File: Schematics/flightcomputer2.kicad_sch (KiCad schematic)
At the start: 0 parts

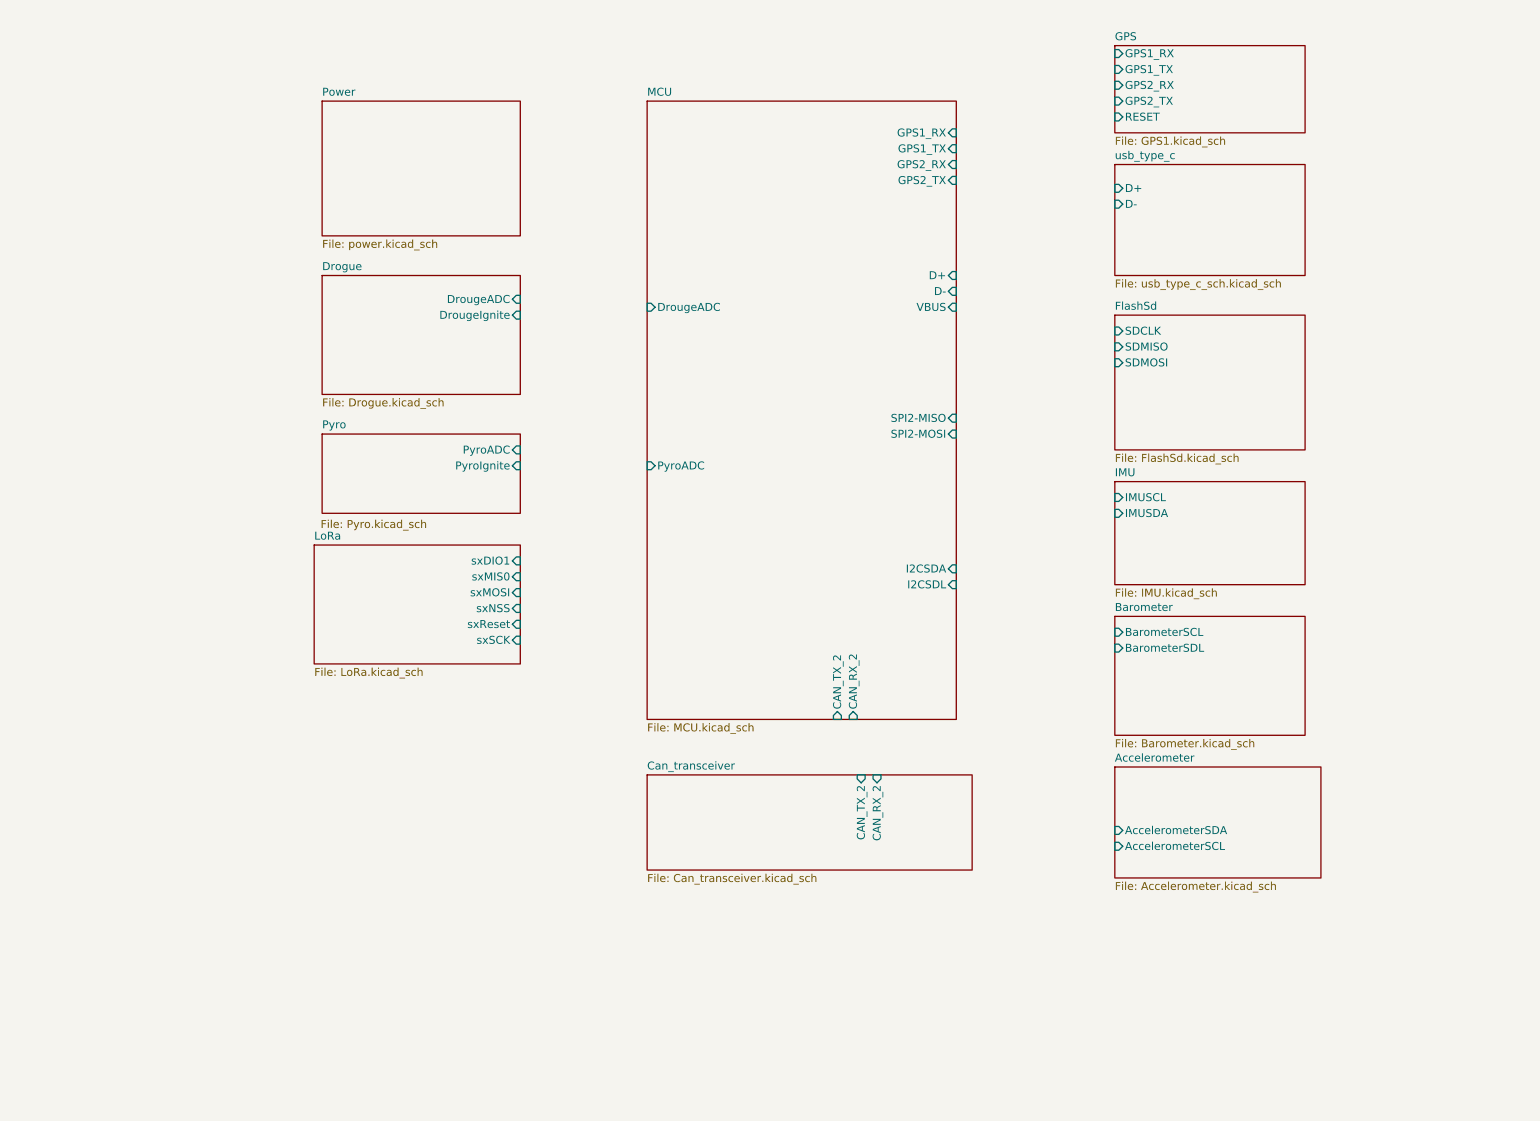
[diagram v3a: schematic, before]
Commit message: finished pin assignments and ran ERC all good ready for layout
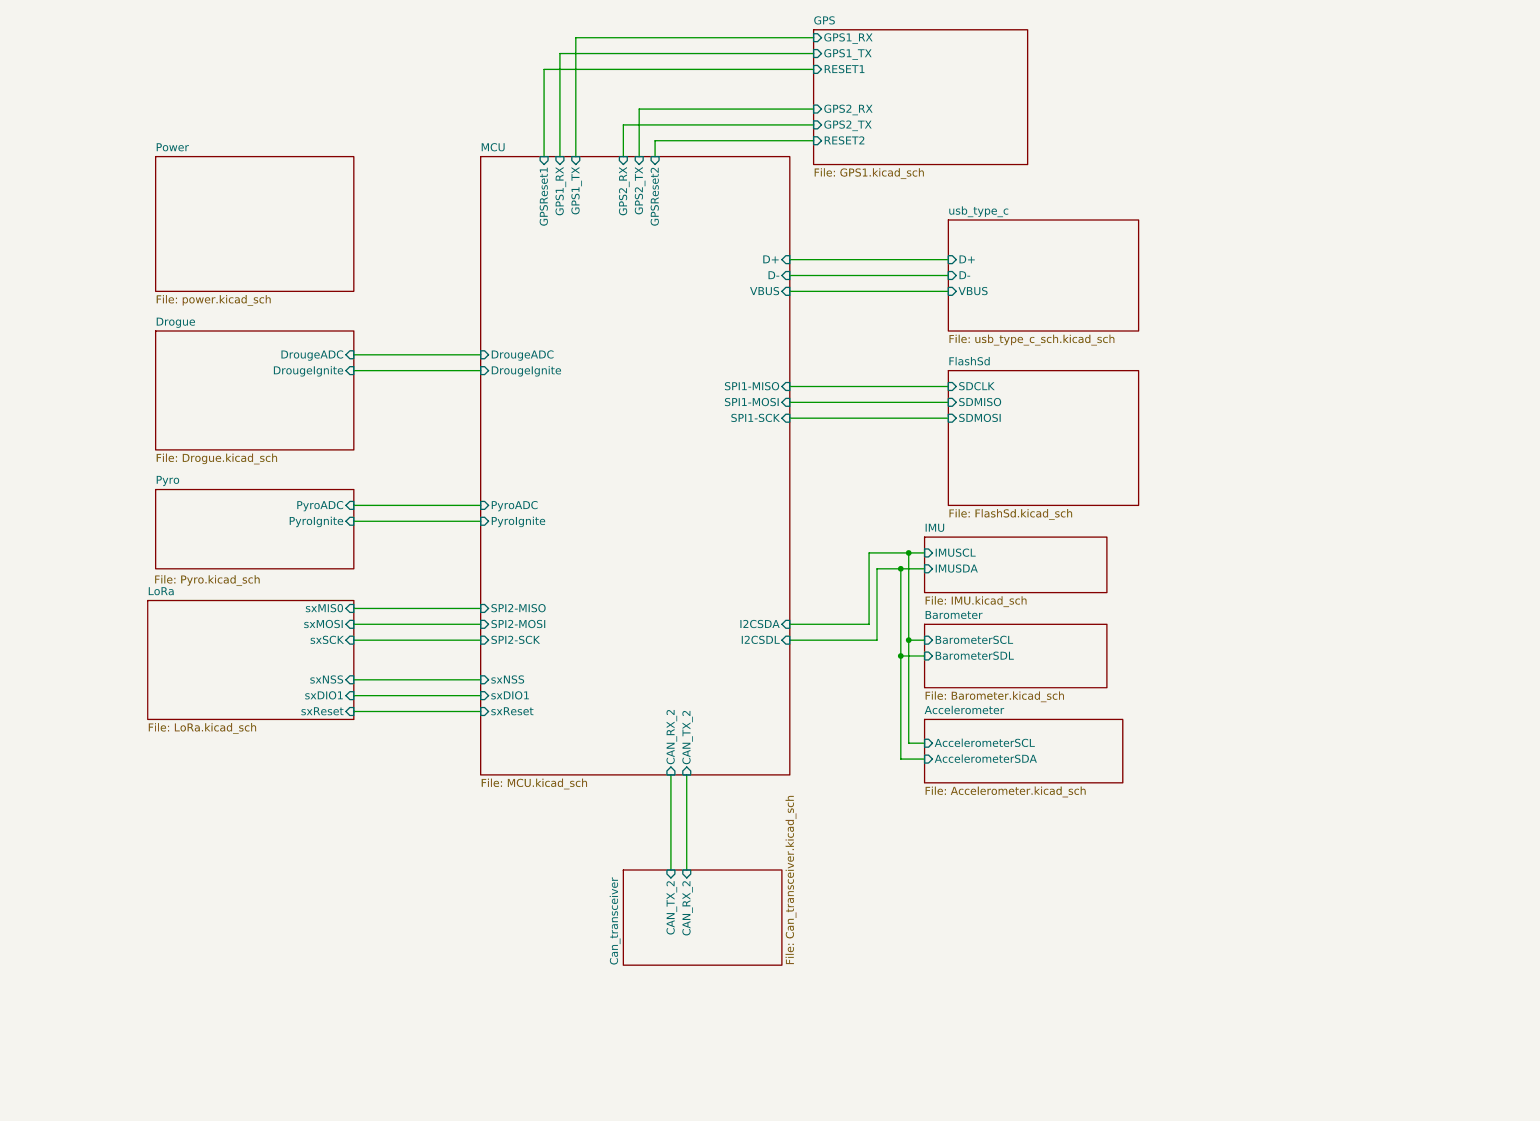
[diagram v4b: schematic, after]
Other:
- sheet GPS ports: added RESET1, RESET2; removed RESET
- sheet MCU ports: added DrougeIgnite, GPSReset1, GPSReset2, PyroIgnite, SPI1-MISO, SPI1-MOSI, SPI1-SCK, SPI2-SCK, sxDIO1, sxNSS, sxReset; removed none
- sheet usb_type_c ports: added VBUS; removed none

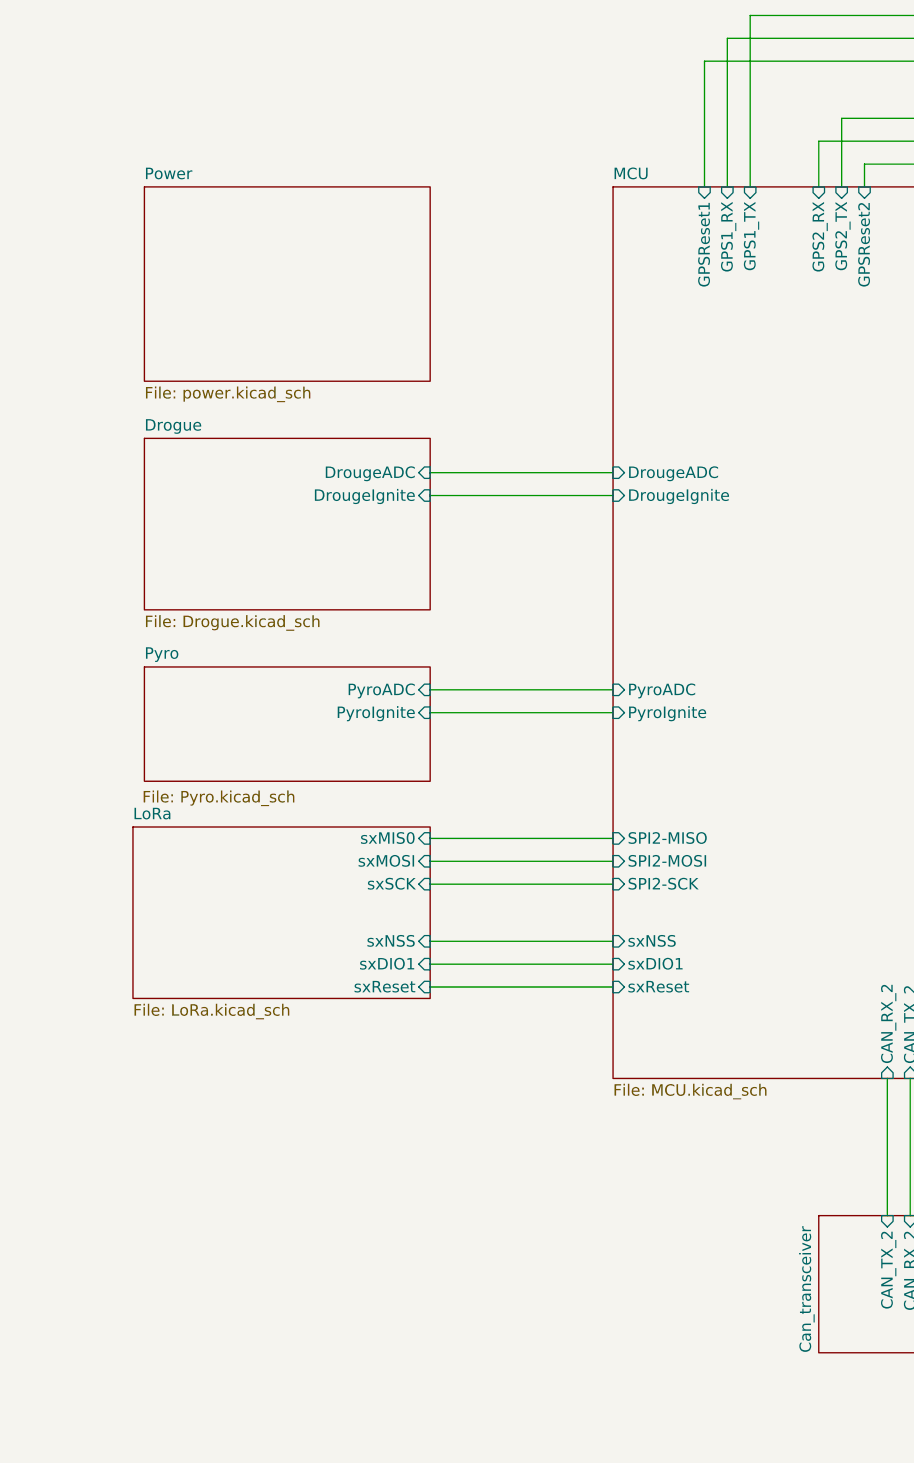
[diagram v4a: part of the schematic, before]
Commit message: Added Flash memory
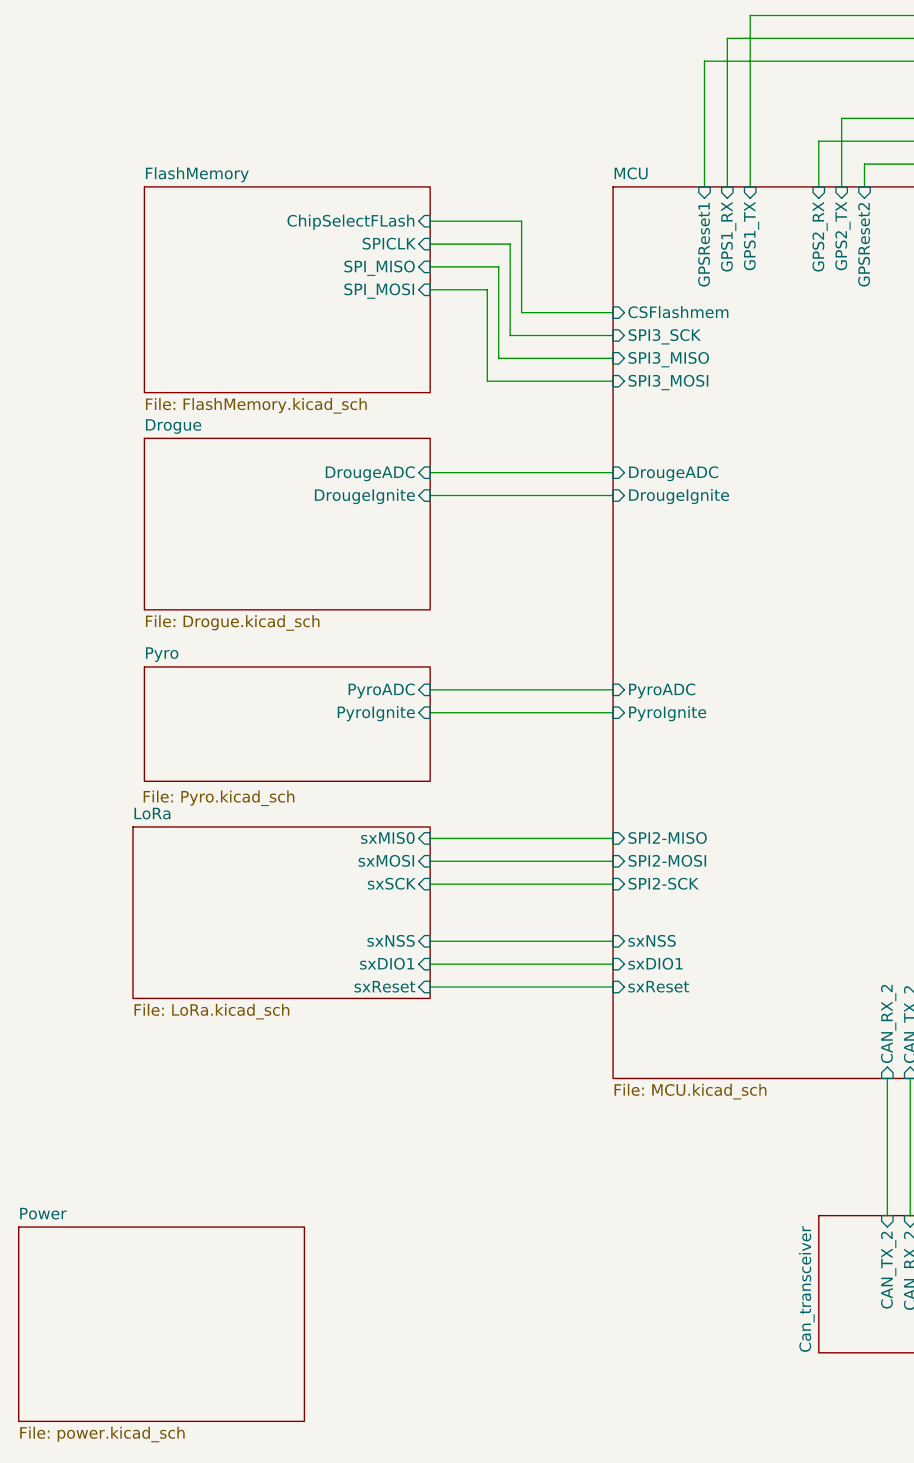
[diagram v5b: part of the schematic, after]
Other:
- added sheet FlashMemory (FlashMemory.kicad_sch)
- sheet MCU ports: added CSFlashmem, SPI3_MISO, SPI3_MOSI, SPI3_SCK; removed none
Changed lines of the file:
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@@
+	(wire
+		(pts
+			(xy 99.06 59.69) (xy 85.09 59.69)
+		)
+		(stroke
+			(width 0)
+			(type default)
+		)
+	)
 	(wire
 		(pts
@@
 	(wire
 		(pts
+			(xy 85.09 49.53) (xy 78.74 49.53)
+		)
+		(stroke
+			(width 0)
+			(type default)
+		)
+	)
+	(wire
+		(pts
 			(xy 121.92 33.02) (xy 152.4 33.02)
 		)
@@
 	(wire
 		(pts
+			(xy 86.36 46.99) (xy 78.74 46.99)
+		)
+		(stroke
+			(width 0)
+			(type default)
+		)
+	)
+	(wire
+		(pts
 			(xy 78.74 115.57) (xy 99.06 115.57)
 		)
@@
 	(wire
 		(pts
+			(xy 87.63 54.61) (xy 87.63 44.45)
+		)
+		(stroke
+			(width 0)
+			(type default)
+		)
+	)
+	(wire
+		(pts
 			(xy 78.74 124.46) (xy 99.06 124.46)
 		)
@@
 	(wire
 		(pts
+			(xy 86.36 57.15) (xy 86.36 46.99)
+		)
+		(stroke
+			(width 0)
+			(type default)
+		)
+	)
+	(wire
+		(pts
+			(xy 88.9 41.91) (xy 78.74 41.91)
+		)
+		(stroke
+			(width 0)
+			(type default)
+		)
+	)
+	(wire
+		(pts
 			(xy 162.56 115.57) (xy 162.56 104.14)
 		)
@@
 	(wire
 		(pts
+			(xy 99.06 52.07) (xy 88.9 52.07)
+		)
+		(stroke
+			(width 0)
+			(type default)
+		)
+	)
+	(wire
+		(pts
 			(xy 129.54 137.16) (xy 129.54 152.4)
 		)
@@
 	(wire
 		(pts
+			(xy 88.9 52.07) (xy 88.9 41.91)
+		)
+		(stroke
+			(width 0)
+			(type default)
+		)
+	)
+	(wire
+		(pts
+			(xy 87.63 44.45) (xy 78.74 44.45)
+		)
+		(stroke
+			(width 0)
+			(type default)
+		)
+	)
+	(wire
+		(pts
+			(xy 99.06 57.15) (xy 86.36 57.15)
+		)
+		(stroke
+			(width 0)
+			(type default)
+		)
+	)
+	(wire
+		(pts
 			(xy 121.92 38.1) (xy 121.92 33.02)
 		)
@@
 	(wire
 		(pts
+			(xy 85.09 59.69) (xy 85.09 49.53)
+		)
+		(stroke
+			(width 0)
+			(type default)
+		)
+	)
+	(wire
+		(pts
 			(xy 166.37 104.14) (xy 170.18 104.14)
+		)
+		(stroke
+			(width 0)
+			(type default)
+		)
+	)
+	(wire
+		(pts
+			(xy 99.06 54.61) (xy 87.63 54.61)
 		)
 		(stroke
@@
 			)
 		)
+		(pin "SPI3_MISO" input
+			(at 99.06 57.15 180)
+			(effects
+				(font
+					(size 1.27 1.27)
+				)
+				(justify left)
+			)
+		)
+		(pin "SPI3_MOSI" input
+			(at 99.06 59.69 180)
+			(effects
+				(font
+					(size 1.27 1.27)
+				)
+				(justify left)
+			)
+		)
+		(pin "SPI3_SCK" input
+			(at 99.06 54.61 180)
+			(effects
+				(font
+					(size 1.27 1.27)
+				)
+				(justify left)
+			)
+		)
+		(pin "CSFlashmem" input
+			(at 99.06 52.07 180)
+			(effects
+				(font
+					(size 1.27 1.27)
+				)
+				(justify left)
+			)
+		)
 		(instances
 			(project "flightcomputer2"
@@
 	)
 	(sheet
+		(at 46.99 38.1)
+		(size 31.75 22.86)
+		(exclude_from_sim no)
+		(in_bom yes)
+		(on_board yes)
+		(dnp no)
+		(fields_autoplaced yes)
+		(stroke
+			(width 0.1524)
+			(type solid)
+		)
+		(fill
+			(color 0 0 0 0.0000)
+		)
+		(property "Sheetname" "FlashMemory"
+			(at 46.99 37.3884 0)
+			(effects
+				(font
+					(size 1.27 1.27)
+				)
+				(justify left bottom)
+			)
+		)
+		(property "Sheetfile" "FlashMemory.kicad_sch"
+			(at 46.99 61.5446 0)
+			(effects
+				(font
+					(size 1.27 1.27)
+				)
+				(justify left top)
+			)
+		)
+		(pin "ChipSelectFLash" input
+			(at 78.74 41.91 0)
+			(effects
+				(font
+					(size 1.27 1.27)
+				)
+				(justify right)
+			)
+		)
+		(pin "SPICLK" input
+			(at 78.74 44.45 0)
+			(effects
+				(font
+					(size 1.27 1.27)
+				)
+				(justify right)
+			)
+		)
+		(pin "SPI_MISO" input
+			(at 78.74 46.99 0)
+			(effects
+				(font
+					(size 1.27 1.27)
+				)
+				(justify right)
+			)
+		)
+		(pin "SPI_MOSI" input
+			(at 78.74 49.53 0)
+			(effects
+				(font
+					(size 1.27 1.27)
+				)
+				(justify right)
+			)
+		)
+		(instances
+			(project "flightcomputer2"
+				(path "/6cb3dda3-5fe8-4715-b831-354360aa3199"
+					(page "14")
+				)
+			)
+		)
+	)
+	(sheet
 		(at 170.18 113.03)
 		(size 29.21 10.16)
@@
 	)
 	(sheet
-		(at 46.99 38.1)
+		(at 33.02 153.67)
 		(size 31.75 21.59)
 		(exclude_from_sim no)
@@
 		)
 		(property "Sheetname" "Power"
-			(at 46.99 37.3884 0)
+			(at 33.02 152.9584 0)
 			(effects
 				(font
@@
 		)
 		(property "Sheetfile" "power.kicad_sch"
-			(at 46.99 60.2746 0)
-			(effects
-				(font
+			(at 33.02 175.8446 0)
+			(effects
+				(font
